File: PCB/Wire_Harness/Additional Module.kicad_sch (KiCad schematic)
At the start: 2 parts, among them J13 Motor Controller 12-pin, J14 Motor Controller 20-pin

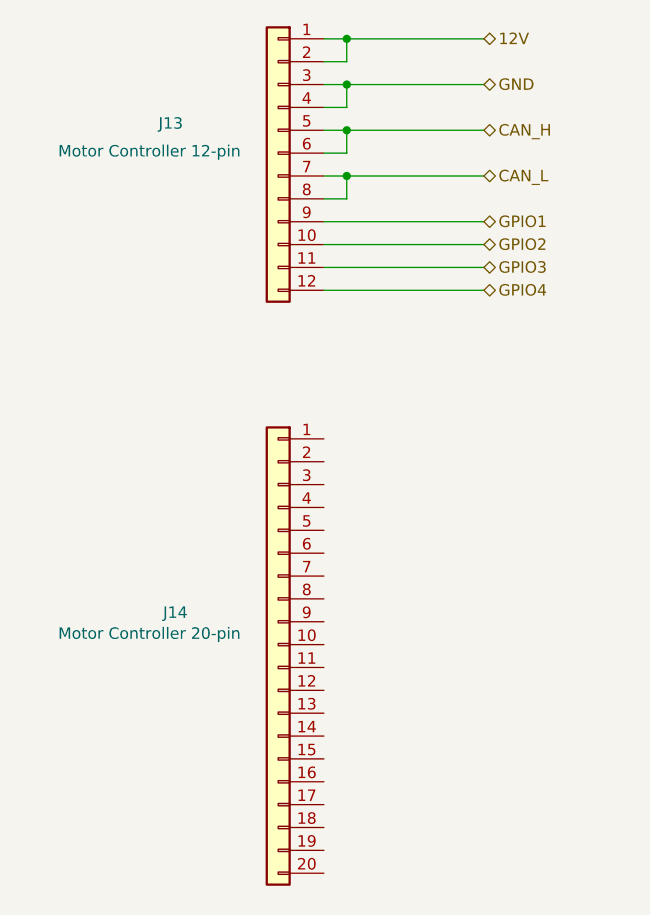
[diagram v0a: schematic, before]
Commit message: changed schematic size to 11x17, added part numbers for enclosures and connectors
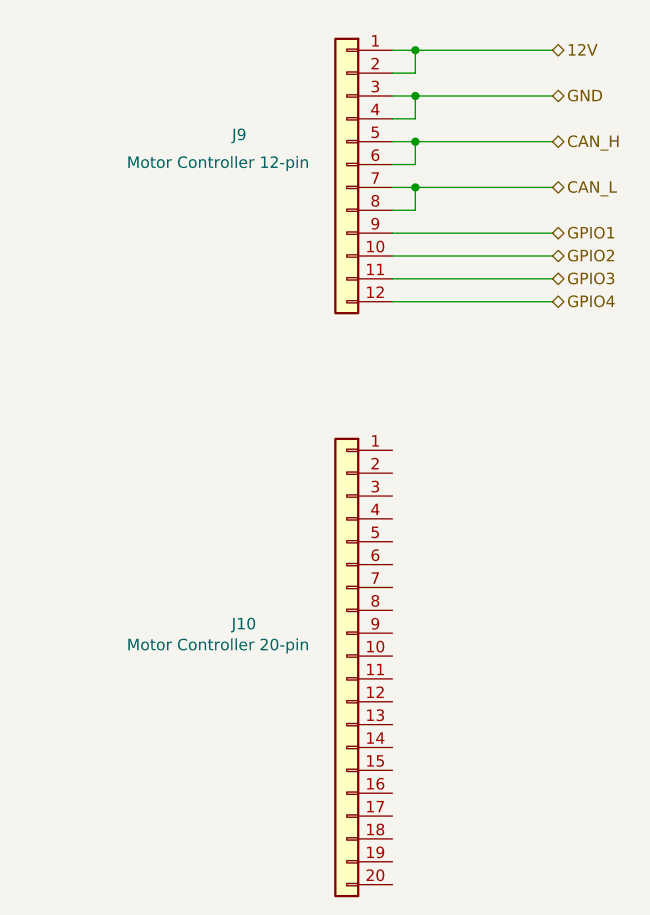
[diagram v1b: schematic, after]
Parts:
- removed J13: Motor Controller 12-pin, symbol VMS_Symbols:Conn_01x12
- removed J14: Motor Controller 20-pin, symbol VMS_Symbols:Conn_01x20
- added J10: Motor Controller 20-pin, symbol VMS_Symbols:Conn_01x20
- added J9: Motor Controller 12-pin, symbol VMS_Symbols:Conn_01x12
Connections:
- net 12V: now also J9.1 (Pin_1), J9.2 (Pin_2)
- net CAN_H: now also J9.5 (Pin_5), J9.6 (Pin_6)
- net CAN_L: now also J9.7 (Pin_7), J9.8 (Pin_8)
- net GND: now also J9.3 (Pin_3), J9.4 (Pin_4)
- net GPIO1: now also J9.9 (Pin_9)
- net GPIO2: now also J9.10 (Pin_10)
- net GPIO3: now also J9.11 (Pin_11)
- net GPIO4: now also J9.12 (Pin_12)
